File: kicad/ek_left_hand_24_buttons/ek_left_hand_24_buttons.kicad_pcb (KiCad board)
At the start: 2 copper layers, 152.6 x 115.9 mm, 68 parts, among them J1 Conn_01x07, J2 Conn_01x06, J3 Conn_01x02, J4 Conn_01x02, M1 MountingHole_3.2mm_M3, M2 MountingHole_3.2mm_M3, M3 MountingHole_3.2mm_M3, M4 MountingHole_3.2mm_M3, U1 74HC165, U2 74HC165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

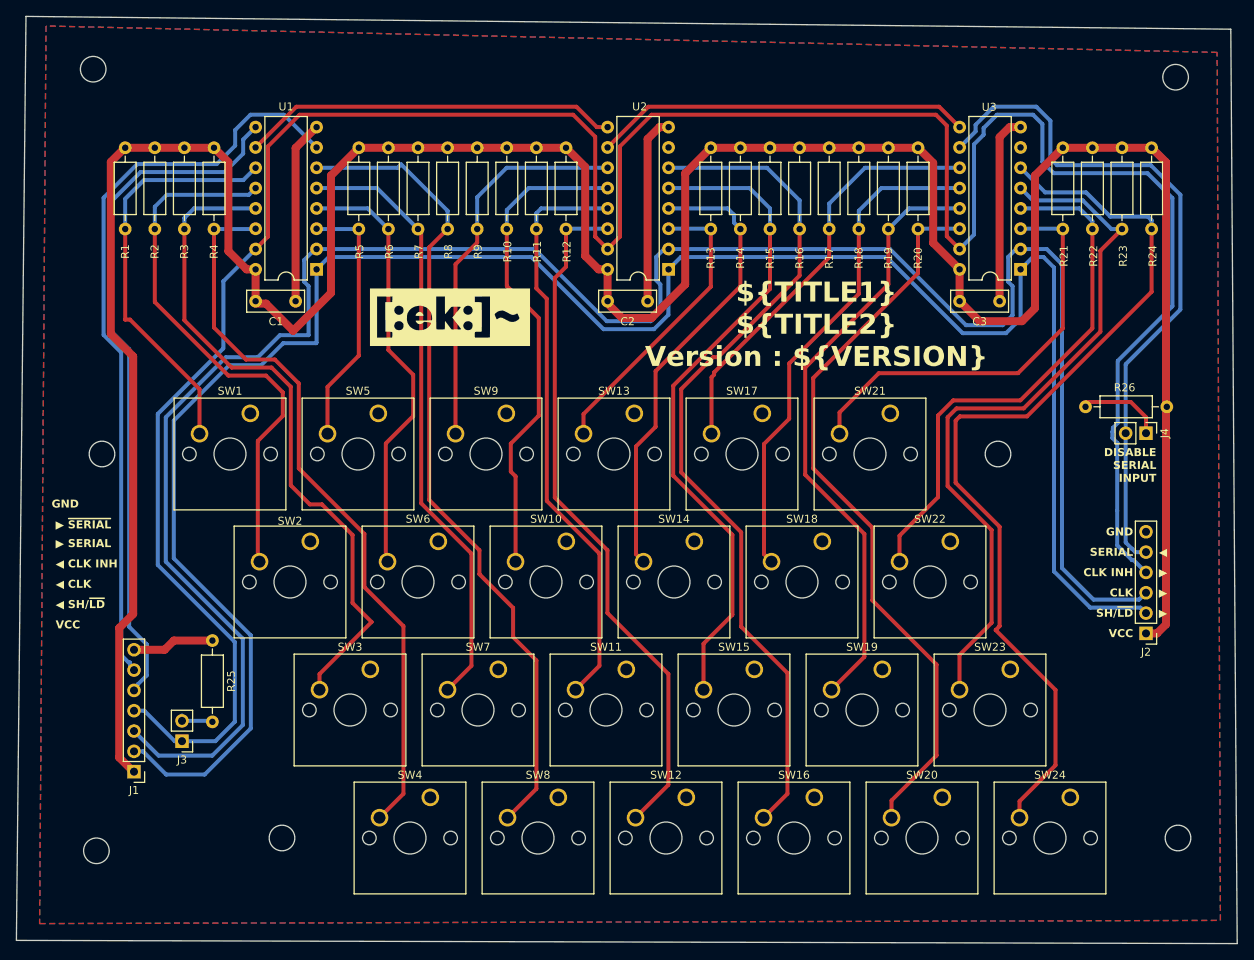
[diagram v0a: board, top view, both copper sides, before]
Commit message: Left hand 24 buttons (first version)
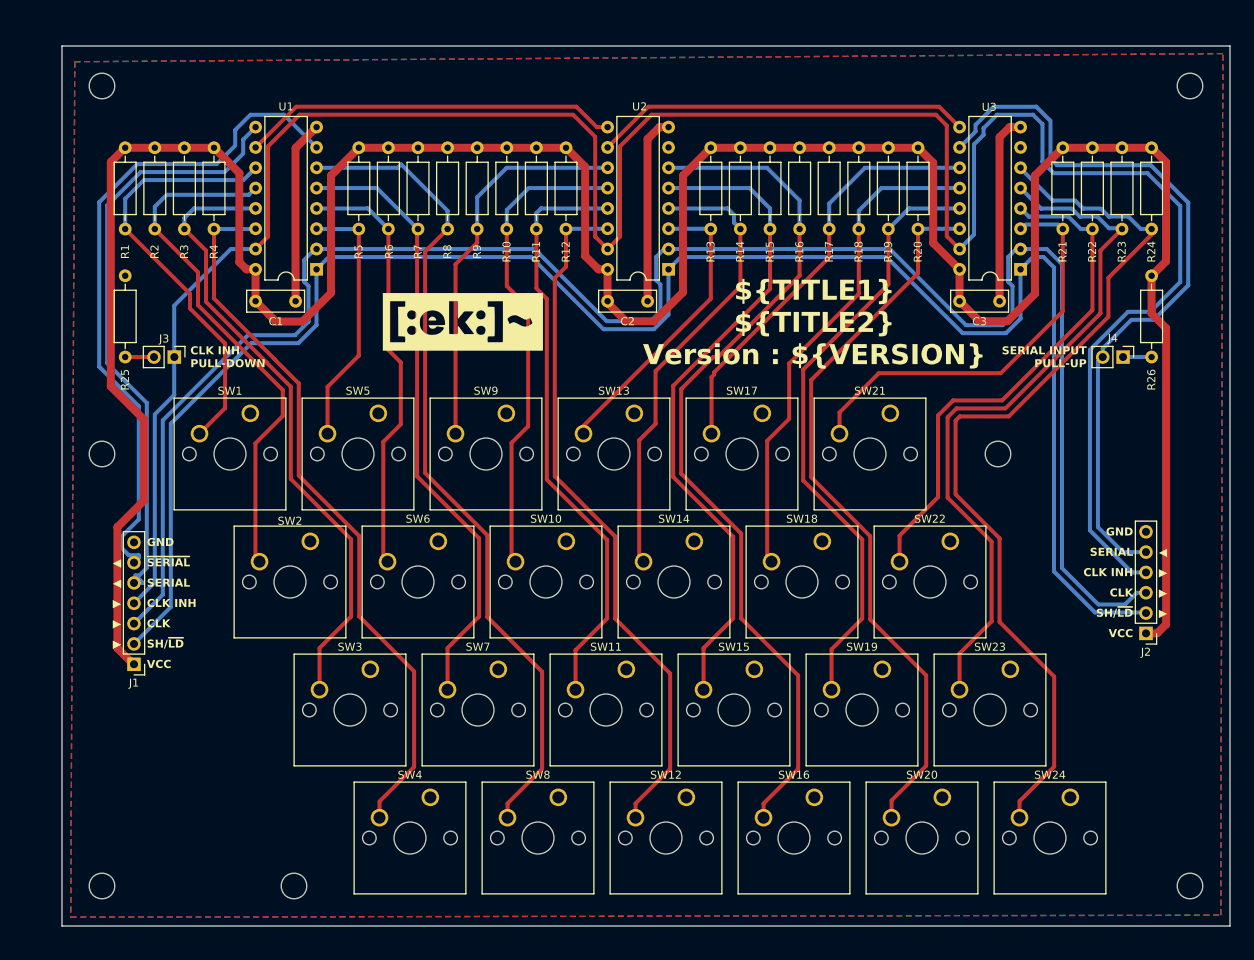
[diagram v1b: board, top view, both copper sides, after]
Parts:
- moved J3 48.0 mm to (56.6, 76.3), turned to -90 degrees
- moved R25 46.9 mm to (50.5, 66.1)
- moved R26 16.5 mm to (178.8, 66.1), turned to -90 degrees
- moved J1 13.4 mm to (51.6, 114.7)
- moved J4 9.94 mm to (175.2, 76.3)
- moved M1 6.18 mm to (71.6, 142.4)
- moved M4 6.18 mm to (183.6, 142.4)
- moved M4 4.46 mm to (47.6, 142.4)
- moved M3 2.37 mm to (47.6, 42.4)
- moved M2 2.11 mm to (183.6, 42.4)
- moved ? 1.71 mm to (92.7, 71.9)
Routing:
- net CLK: track 262.3 -> 230.4 mm
- net SH/~{LD}: track 259.0 -> 227.0 mm
- net CLK INH: track 327.3 -> 302.0 mm
- net VCC: track 380.0 -> 368.1 mm
- net GND: track 80.7 -> 70.4 mm
- net /Buttons 01-08/SERIAL_OUT: track 85.5 -> 75.3 mm
- net /Buttons 01-08/~{SERIAL_OUT}: track 94.5 -> 84.5 mm
- net Net-(J4-Pin_1): track 10.5 -> 3.00 mm
- net /Buttons 17-24/SERIAL_IN: track 86.8 -> 93.1 mm
- net Net-(U1-D2): track 84.6 -> 78.6 mm
- net Net-(U1-D1): track 68.7 -> 66.2 mm
- net Net-(U3-D7): track 116.3 -> 113.8 mm
- net Net-(U1-D0): track 51.5 -> 53.8 mm
- net Net-(U3-D5): track 67.6 -> 65.7 mm
- net Net-(U3-D6): track 90.3 -> 88.9 mm
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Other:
- board size 152.6 x 115.9 mm -> 146 x 110 mm
- board text added: "CLK INH PULL-DOWN"
- board text added: "SERIAL INPUT PULL-UP"
- board text added: "~{SERIAL}"
- board text removed: "DISABLE SERIAL INPUT"
- board text removed: "▶ SERIAL"
- board text removed: "▶ ~{SERIAL}"
- board text removed: "◀ CLK"
- board text removed: "◀ CLK INH"
- board text removed: "◀ SH/~{LD}"

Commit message: Left Hand 24 before vias
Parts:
- moved J1 5.50 mm to (51.6, 120.2)
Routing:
- net Net-(U3-D7): track 113.8 -> 100.2 mm
- net SH/~{LD}: track 227.0 -> 217.0 mm
- net VCC: track 368.1 -> 376.0 mm
- net CLK: track 230.4 -> 222.8 mm
- net Net-(U3-D6): track 88.9 -> 82.5 mm
- net /Buttons 01-08/SERIAL_OUT: track 75.3 -> 80.5 mm
- net /Buttons 01-08/~{SERIAL_OUT}: track 84.5 -> 89.5 mm
- net Net-(U3-D5): track 65.7 -> 69.7 mm
- net Net-(U1-D3): track 90.9 -> 94.5 mm
- net /Buttons 17-24/SERIAL_IN: track 93.1 -> 89.6 mm
- net Net-(U2-D4): track 37.5 -> 41.0 mm
- net Net-(U1-D4): track 32.5 -> 35.8 mm
- net CLK INH: track 302.0 -> 299.0 mm
- net Net-(U1-D0): track 53.8 -> 51.1 mm
- net Net-(U3-D3): track 92.1 -> 94.4 mm
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
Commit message: Left Hand 24 after vias
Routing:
- net CLK: track 222.8 -> 226.9 mm
- net SH/~{LD}: track 217.0 -> 219.8 mm
- net VCC: track 376.0 -> 378.5 mm
- net Net-(U1-D0): track 51.1 -> 48.9 mm
- net CLK INH: track 299.0 -> 300.7 mm
- net /Buttons 17-24/SERIAL_IN: track 89.6 -> 91.3 mm
- net Net-(U3-D6): track 82.5 -> 81.0 mm
- net /Buttons 01-08/~{SERIAL_OUT}: track 89.5 -> 88.7 mm
- net /Buttons 01-08/SERIAL_OUT: track 80.5 -> 79.9 mm
- net GND: vias 0 -> 211
